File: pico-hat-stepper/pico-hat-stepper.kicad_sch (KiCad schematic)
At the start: 0 parts

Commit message: tmc5160_featherwing -> pico-hat-stepper
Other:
- title: tmc5160_featherwing -> pico-hat-stepper
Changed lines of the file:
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@@
   (paper "A4")
   (title_block
-    (title "tmc5160_featherwing")
+    (title "pico-hat-stepper")
     (date "2024-04-16")
     (rev "1.0")
@@
     )
     (instances
-      (project "tmc5160_featherwing"
+      (project "pico-hat-stepper"
         (path "/df2b2e89-e055-4140-95de-f1df723db034" (page "4"))
       )
@@
     )
     (instances
-      (project "tmc5160_featherwing"
+      (project "pico-hat-stepper"
         (path "/df2b2e89-e055-4140-95de-f1df723db034" (page "2"))
       )
@@
     )
     (instances
-      (project "tmc5160_featherwing"
+      (project "pico-hat-stepper"
         (path "/df2b2e89-e055-4140-95de-f1df723db034" (page "13"))
       )
@@
     )
     (instances
-      (project "tmc5160_featherwing"
+      (project "pico-hat-stepper"
         (path "/df2b2e89-e055-4140-95de-f1df723db034" (page "3"))
       )

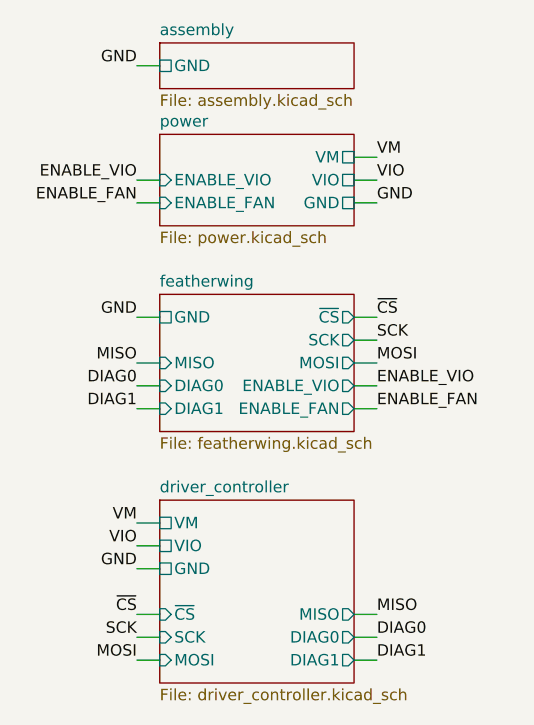
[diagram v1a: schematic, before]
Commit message: featherwing -> pico-hat
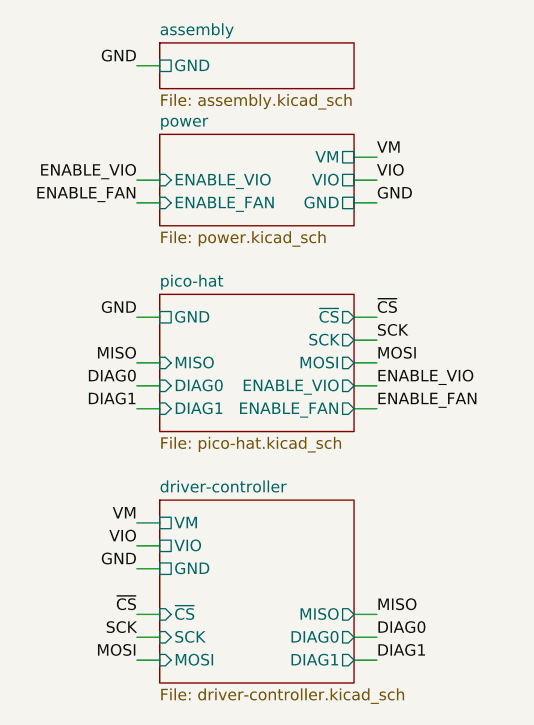
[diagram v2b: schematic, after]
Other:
- sheet driver_controller renamed driver-controller
- sheet featherwing renamed pico-hat
- sheet driver-controller: file driver_controller.kicad_sch -> driver-controller.kicad_sch
- sheet pico-hat: file featherwing.kicad_sch -> pico-hat.kicad_sch
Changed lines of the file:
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@@
     (stroke (width 0.1524) (type solid))
     (fill (color 0 0 0 0.0000))
-    (property "Sheetname" "driver_controller" (at 130.81 107.2384 0)
+    (property "Sheetname" "driver-controller" (at 130.81 107.2384 0)
       (effects (font (size 1.27 1.27)) (justify left bottom))
     )
-    (property "Sheetfile" "driver_controller.kicad_sch" (at 130.81 128.8546 0)
+    (property "Sheetfile" "driver-controller.kicad_sch" (at 130.81 128.8546 0)
       (effects (font (size 1.27 1.27)) (justify left top))
     )
@@
     (stroke (width 0.1524) (type solid))
     (fill (color 0 0 0 0.0000))
-    (property "Sheetname" "featherwing" (at 130.81 84.3784 0)
+    (property "Sheetname" "pico-hat" (at 130.81 84.3784 0)
       (effects (font (size 1.27 1.27)) (justify left bottom))
     )
-    (property "Sheetfile" "featherwing.kicad_sch" (at 130.81 100.9146 0)
+    (property "Sheetfile" "pico-hat.kicad_sch" (at 130.81 100.9146 0)
       (effects (font (size 1.27 1.27)) (justify left top))
     )
